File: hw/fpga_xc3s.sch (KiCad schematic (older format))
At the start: 44 parts, among them J4 JTAG, J5 GPIO2V5, J9 Conn_02x04_Odd_Even, U5 XC3S50A-VQ100, U6 AT25DF041B

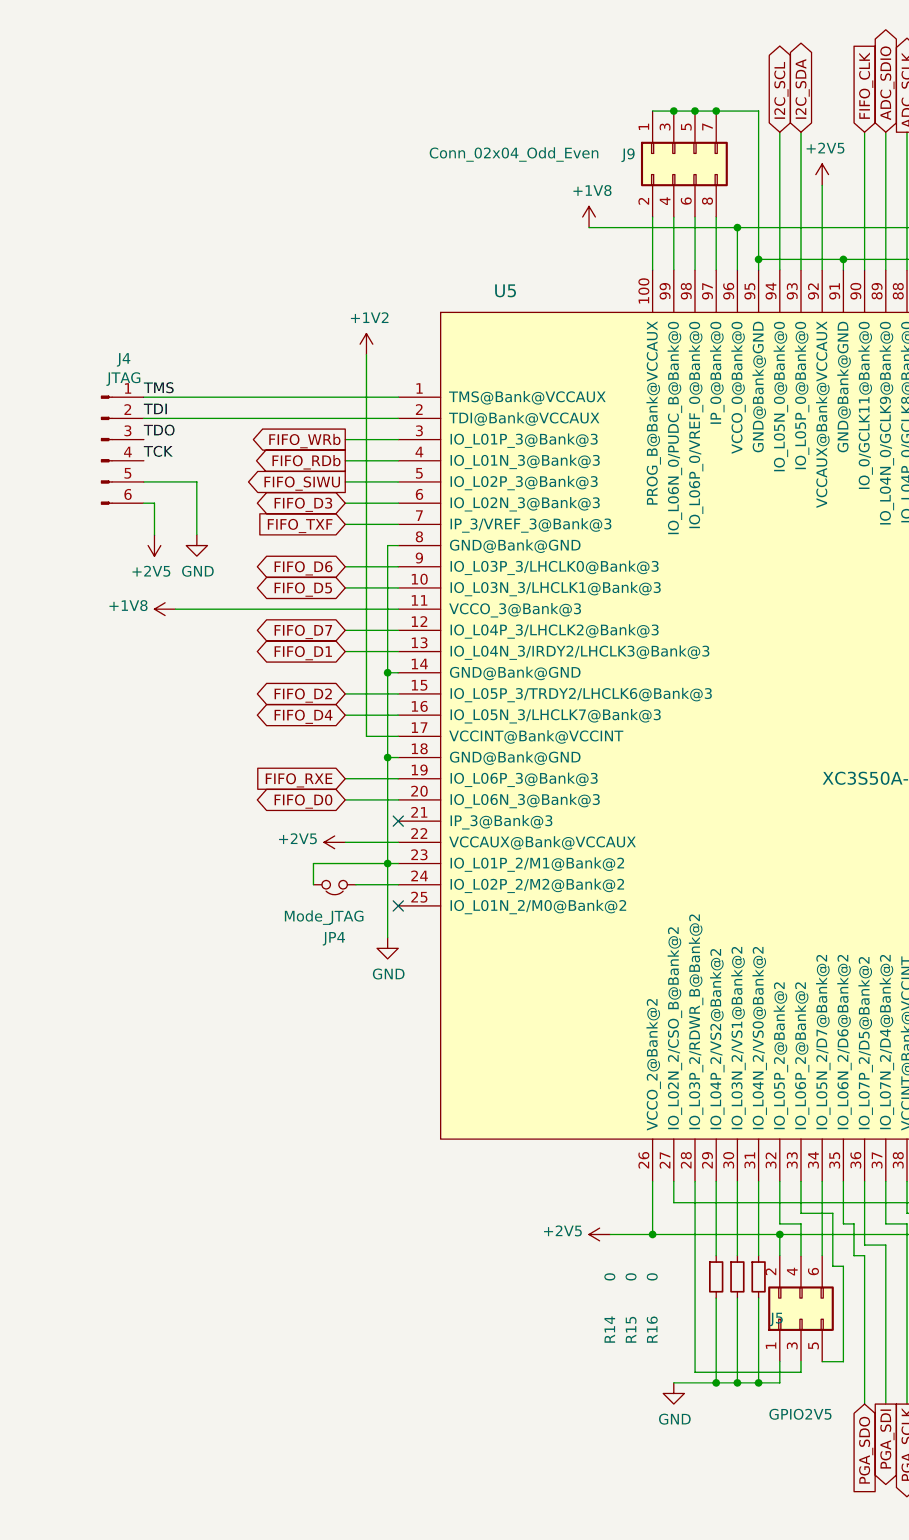
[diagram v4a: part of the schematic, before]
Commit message: everything hooked up + layed out; 0.2/0.4mm vias :-(
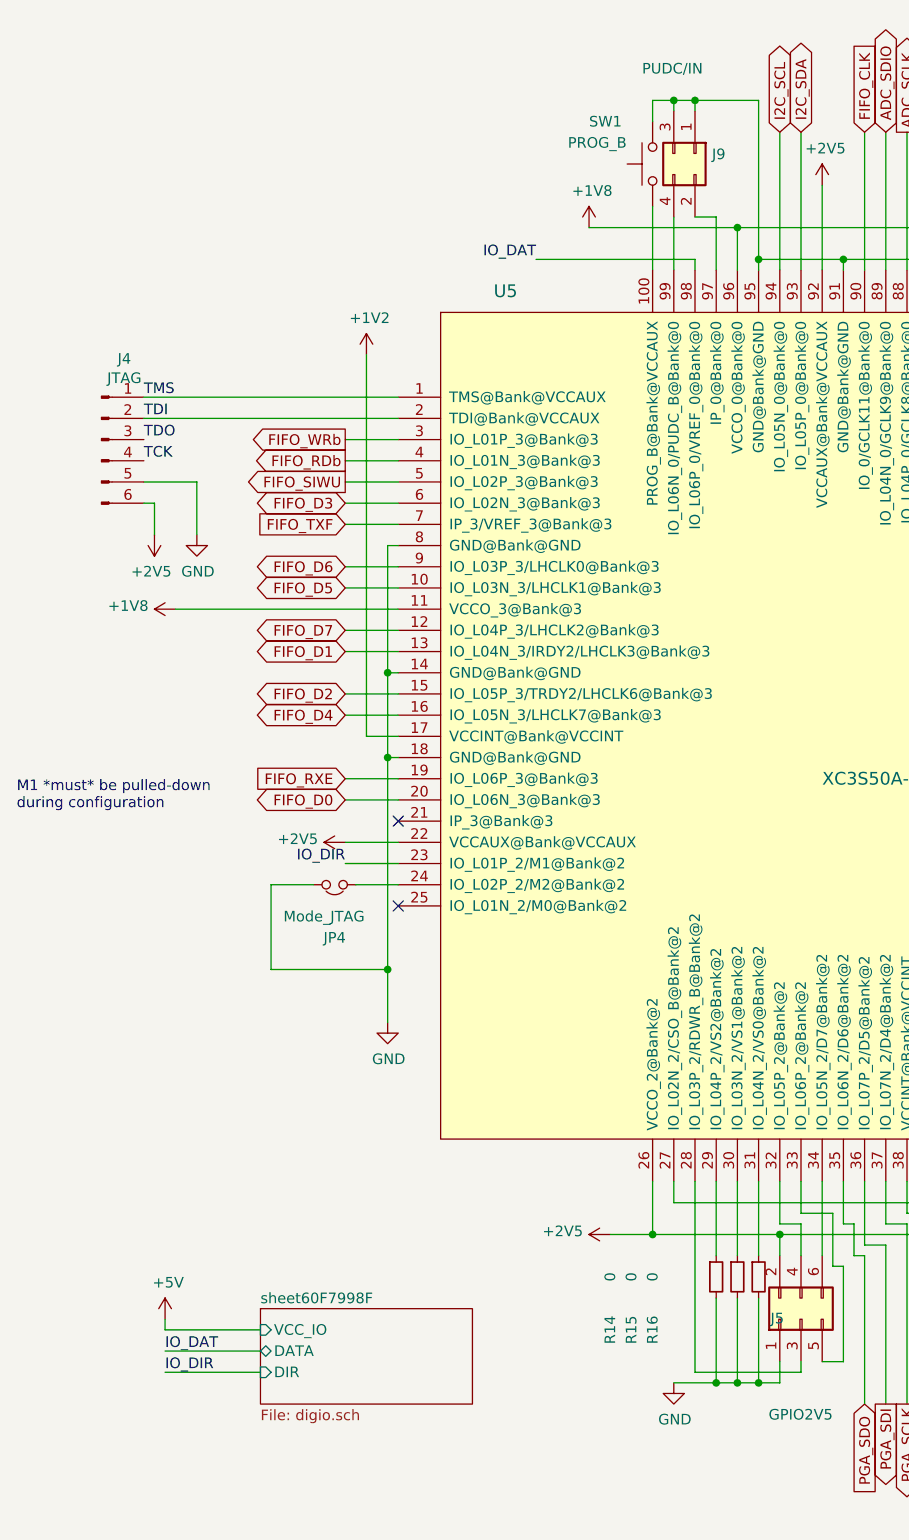
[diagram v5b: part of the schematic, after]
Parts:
- removed J9: Conn_02x04_Odd_Even, Connector_PinHeader_2.54mm:PinHeader_2x04_P2.54mm_Vertical, symbol Connector_Generic:Conn_02x04_Odd_Even
- added J9: PUDC/IN, Connector_PinHeader_2.54mm:PinHeader_2x02_P2.54mm_Vertical, symbol Connector_Generic:Conn_02x02_Odd_Even
- added SW1: PROG_B, Button_Switch_SMD:SW_SPST_PTS810, symbol Switch:SW_Push
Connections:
- net GND: now also J9.1 (Pin_1), J9.3 (Pin_3), SW1.2; no longer U5.23 (IO_L01P_2/M1@Bank@2)
- net at U5.100 (PROG_B@Bank@VCCAUX): now also SW1.1
- net at U5.99 (IO_L06N_0/PUDC_B@Bank@0): now also J9.4 (Pin_4)
- net IO_DAT: now reaches U5.98 (IO_L06P_0/VREF_0@Bank@0)
- net at U5.97 (IP_0@Bank@0): now also J9.2 (Pin_2)
- new net IO_DIR: U5.23 (IO_L01P_2/M1@Bank@2)
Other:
- note added: "M1 *must* be pulled-down\nduring configuration"
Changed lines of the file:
@@
 $Descr A4 11693 8268
 encoding utf-8
-Sheet 3 8
+Sheet 3 9
 Title ""
 Date ""
@@
 L power:GND #PWR?
 U 1 1 60AF9070
-P 2300 4950
+P 2300 5350
 AR Path="/6086F2E3/60AF9070" Ref="#PWR?"  Part="1"
 AR Path="/60AABC24/60AF9070" Ref="#PWR?"  Part="1"
-F 0 "#PWR?" H 2300 4700 50  0001 C CNN
-F 1 "GND" H 2305 4777 50  0000 C CNN
-F 2 "" H 2300 4950 50  0001 C CNN
-F 3 "" H 2300 4950 50  0001 C CNN
-	1    2300 4950
+F 0 "#PWR?" H 2300 5100 50  0001 C CNN
+F 1 "GND" H 2305 5177 50  0000 C CNN
+F 2 "" H 2300 5350 50  0001 C CNN
+F 3 "" H 2300 5350 50  0001 C CNN
+	1    2300 5350
 	1    0    0    -1
 $EndComp
@@
 Wire Wire Line
 	8050 5800 8050 6200
-NoConn ~ 2350 4800
 $Comp
 L Device:Jumper_NC_Small JP4
@@
 $EndComp
 Wire Wire Line
-	2300 4100 2300 4600
-Wire Wire Line
-	2350 4600 2300 4600
-Connection ~ 2300 4600
-Wire Wire Line
-	2300 4600 2300 4950
-Wire Wire Line
-	1950 4700 1950 4600
-Wire Wire Line
-	1950 4600 2300 4600
-Wire Wire Line
 	2350 4700 2150 4700
-Wire Wire Line
-	3550 1550 3550 1800
 $Comp
 L Connector:TestPoint TP1
@@
 $EndComp
 Wire Wire Line
-	3750 1550 3750 1800
-Wire Wire Line
 	3850 1550 3850 1800
-$Comp
-L Connector_Generic:Conn_02x04_Odd_Even J9
-U 1 1 60AB847C
-P 3650 1250
-F 0 "J9" V 3654 1430 50  0000 L CNN
-F 1 "Conn_02x04_Odd_Even" V 3650 1600 50  0000 L CNN
-F 2 "Connector_PinHeader_2.54mm:PinHeader_2x04_P2.54mm_Vertical" H 3650 1250 50  0001 C CNN
-F 3 "~" H 3650 1250 50  0001 C CNN
-	1    3650 1250
-	0    -1   1    0
-$EndComp
-Wire Wire Line
-	3550 1050 3650 1050
-Wire Wire Line
-	4050 1050 4050 1750
-Connection ~ 3650 1050
-Wire Wire Line
-	3650 1050 3750 1050
-Connection ~ 3750 1050
-Wire Wire Line
-	3750 1050 3850 1050
-Connection ~ 3850 1050
-Wire Wire Line
-	3850 1050 4050 1050
 Connection ~ 4050 1750
 Wire Wire Line
@@
 Wire Wire Line
 	4250 6250 4400 6250
+$Sheet
+S 1700 6700 1000 450
+U 60F79994
+F0 "sheet60F7998F" 50
+F1 "digio.sch" 50
+F2 "DATA" B L 1700 6900 50
+F3 "DIR" I L 1700 7000 50
+F4 "VCC_IO" I L 1700 6800 50
+$EndSheet
+Wire Wire Line
+	1700 6900 1250 6900
+Wire Wire Line
+	1700 7000 1250 7000
+Text Label 1250 6900 0    50   ~ 0
+IO_DAT
+Text Label 1250 7000 0    50   ~ 0
+IO_DIR
+$Comp
+L power:+5V #PWR?
+U 1 1 60FB29D3
+P 1250 6750
+AR Path="/6086F2E3/60FB29D3" Ref="#PWR?"  Part="1"
+AR Path="/60AABC24/60FB29D3" Ref="#PWR?"  Part="1"
+F 0 "#PWR?" H 1250 6600 50  0001 C CNN
+F 1 "+5V" H 1265 6923 50  0000 C CNN
+F 2 "" H 1250 6750 50  0001 C CNN
+F 3 "" H 1250 6750 50  0001 C CNN
+	1    1250 6750
+	1    0    0    -1
+$EndComp
+Wire Wire Line
+	1700 6800 1250 6800
+Wire Wire Line
+	1250 6800 1250 6750
+NoConn ~ 2350 4800
+Text Notes 550  4350 0    50   ~ 0
+M1 *must* be pulled-down\nduring configuration
+Wire Wire Line
+	1950 4700 1750 4700
+Wire Wire Line
+	1750 5100 2300 5100
+Wire Wire Line
+	1750 4700 1750 5100
+Connection ~ 2300 5100
+Wire Wire Line
+	2300 5100 2300 5350
+Wire Wire Line
+	2300 4100 2300 5100
+Wire Wire Line
+	2350 4600 2100 4600
+Text Label 2100 4600 2    50   ~ 0
+IO_DIR
+Wire Wire Line
+	4050 1000 3750 1000
+Wire Wire Line
+	4050 1000 4050 1750
+Wire Wire Line
+	3650 1050 3650 1000
+Connection ~ 3650 1000
+Wire Wire Line
+	3650 1000 3550 1000
+Wire Wire Line
+	3750 1050 3750 1000
+Connection ~ 3750 1000
+Wire Wire Line
+	3750 1000 3650 1000
+Wire Wire Line
+	3750 1550 3850 1550
+Wire Wire Line
+	3750 1800 3750 1750
+Wire Wire Line
+	3750 1750 3000 1750
+Text Label 3000 1750 2    50   ~ 0
+IO_DAT
+$Comp
+L Connector_Generic:Conn_02x02_Odd_Even J9
+U 1 1 61188A24
+P 3750 1250
+F 0 "J9" V 3754 1330 50  0000 L CNN
+F 1 "PUDC/IN" V 3350 1000 50  0000 L CNN
+F 2 "Connector_PinHeader_2.54mm:PinHeader_2x02_P2.54mm_Vertical" H 3750 1250 50  0001 C CNN
+F 3 "~" H 3750 1250 50  0001 C CNN
+	1    3750 1250
+	0    1    1    0
+$EndComp
+$Comp
+L Switch:SW_Push SW1
+U 1 1 61189FCC
+P 3550 1300
+F 0 "SW1" V 3750 1600 50  0000 R CNN
+F 1 "PROG_B" V 3650 1700 50  0000 R CNN
+F 2 "Button_Switch_SMD:SW_SPST_PTS810" H 3550 1500 50  0001 C CNN
+F 3 "~" H 3550 1500 50  0001 C CNN
+	1    3550 1300
+	0    -1   -1   0
+$EndComp
+Wire Wire Line
+	3550 1000 3550 1100
+Wire Wire Line
+	3550 1500 3550 1800
 $EndSCHEMATC

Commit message: prototype version
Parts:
- removed J9: PUDC/IN, Connector_PinHeader_2.54mm:PinHeader_2x02_P2.54mm_Vertical, symbol Connector_Generic:Conn_02x02_Odd_Even
- added D15: LED_Front, proj_footprints:LED_Wuerth_Sideview, symbol Device:LED_Dual_CAC
- added J12: PUDC_B/IN, Connector_PinHeader_2.54mm:PinHeader_2x02_P2.54mm_Vertical, symbol Connector_Generic:Conn_02x02_Odd_Even
- added R83, R84: 1k5, Resistor_SMD:R_0603_1608Metric, symbol Device:R_Small
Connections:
- net +2V5: now also D15.2 (A)
- net GND: now also U5.23 (IO_L01P_2/M1@Bank@2), J12.2 (Pin_2), J12.4 (Pin_4)
- net IO_DIR: now also U5.71 (IO_L05N_1@Bank@1); no longer U5.23 (IO_L01P_2/M1@Bank@2)
- net at U5.25 (IO_L01N_2/M0@Bank@2): now also R83.1
- net LED_FRONT_G: now reaches U5.52 (IO_L12P_2/D1@Bank@2)
- net LED_FRONT_G: now also R84.1
- net at U5.72 (IO_L06P_1@Bank@1): now also U5.73 (IO_L06N_1@Bank@1); no longer U5.71 (IO_L05N_1@Bank@1)
- net EXP_IO1_1V8: now reaches U5.77 (IO_L01P_0/VREF_0@Bank@0)
- net EXP_IO2_1V8: now reaches U5.78 (IO_L01N_0@Bank@0)
- net at U5.97 (IP_0@Bank@0): now also J12.3 (Pin_3)
- net at U5.99 (IO_L06N_0/PUDC_B@Bank@0): now also J12.1 (Pin_1)
- new net: D15.1 (K1), R83.2
- new net: D15.3 (K2), R84.2
- no-connect marks 9 -> 4
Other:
- note added: "M1 *must* be pulled-down,\nM0 *must* be pulled-up\nduring configuration;"
- note removed: "M1 *must* be pulled-down\nduring configuration"
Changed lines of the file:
@@
 U 1 1 6089B5A3
 P 7450 4600
-F 0 "R18" V 7700 4600 50  0000 C CNN
-F 1 "50" V 7550 4600 50  0000 C CNN
+F 0 "R18" V 7400 4450 50  0000 C CNN
+F 1 "50" V 7400 4750 50  0000 C CNN
 F 2 "Resistor_SMD:R_0603_1608Metric" H 7450 4600 50  0001 C CNN
 F 3 "~" H 7450 4600 50  0001 C CNN
@@
 Text GLabel 4550 1150 1    50   Input ~ 0
 FIFO_CLK
-NoConn ~ 7150 4700
 Wire Wire Line
 	3850 6650 3850 7050
@@
 Wire Wire Line
 	5150 1150 5150 1800
-NoConn ~ 5750 1800
-NoConn ~ 5850 1800
 Wire Wire Line
 	4250 1150 4250 1800
@@
 	1    0    0    -1
 $EndComp
-Wire Wire Line
-	3850 1550 3850 1800
-Connection ~ 4050 1750
 Wire Wire Line
 	4050 1750 4050 1800
@@
 Wire Wire Line
 	7150 3200 8100 3200
-Wire Wire Line
-	7150 2700 7450 2700
-Wire Wire Line
-	7450 2700 7450 2800
-Wire Wire Line
-	7450 2800 7150 2800
-NoConn ~ 7150 2600
 Text GLabel 2100 3300 0    50   BiDi ~ 0
 FIFO_D5
@@
 	4250 6250 4400 6250
 $Sheet
-S 1700 6700 1000 450
+S 1700 6700 850  600
 U 60F79994
 F0 "sheet60F7998F" 50
@@
 F2 "DATA" B L 1700 6900 50
 F3 "DIR" I L 1700 7000 50
-F4 "VCC_IO" I L 1700 6800 50
+F4 "VCC_IO" I R 2550 6800 50
+F5 "VCC_LOGIC" I L 1700 6800 50
 $EndSheet
 Wire Wire Line
@@
 L power:+5V #PWR?
 U 1 1 60FB29D3
-P 1250 6750
+P 2700 6650
 AR Path="/6086F2E3/60FB29D3" Ref="#PWR?"  Part="1"
 AR Path="/60AABC24/60FB29D3" Ref="#PWR?"  Part="1"
-F 0 "#PWR?" H 1250 6600 50  0001 C CNN
-F 1 "+5V" H 1265 6923 50  0000 C CNN
-F 2 "" H 1250 6750 50  0001 C CNN
-F 3 "" H 1250 6750 50  0001 C CNN
-	1    1250 6750
+F 0 "#PWR?" H 2700 6500 50  0001 C CNN
+F 1 "+5V" H 2715 6823 50  0000 C CNN
+F 2 "" H 2700 6650 50  0001 C CNN
+F 3 "" H 2700 6650 50  0001 C CNN
+	1    2700 6650
 	1    0    0    -1
 $EndComp
@@
 Wire Wire Line
 	1250 6800 1250 6750
-NoConn ~ 2350 4800
 Text Notes 550  4350 0    50   ~ 0
-M1 *must* be pulled-down\nduring configuration
+M1 *must* be pulled-down,\nM0 *must* be pulled-up\nduring configuration;
 Wire Wire Line
 	1950 4700 1750 4700
@@
 	2300 5100 2300 5350
 Wire Wire Line
-	2300 4100 2300 5100
-Wire Wire Line
-	2350 4600 2100 4600
-Text Label 2100 4600 2    50   ~ 0
+	2300 4100 2300 4600
+Text Label 7600 2800 0    50   ~ 0
 IO_DIR
 Wire Wire Line
-	4050 1000 3750 1000
-Wire Wire Line
-	4050 1000 4050 1750
-Wire Wire Line
 	3650 1050 3650 1000
-Connection ~ 3650 1000
 Wire Wire Line
 	3650 1000 3550 1000
-Wire Wire Line
-	3750 1050 3750 1000
-Connection ~ 3750 1000
-Wire Wire Line
-	3750 1000 3650 1000
-Wire Wire Line
-	3750 1550 3850 1550
 Wire Wire Line
 	3750 1800 3750 1750
@@
 IO_DAT
 $Comp
-L Connector_Generic:Conn_02x02_Odd_Even J9
-U 1 1 61188A24
-P 3750 1250
-F 0 "J9" V 3754 1330 50  0000 L CNN
-F 1 "PUDC/IN" V 3350 1000 50  0000 L CNN
-F 2 "Connector_PinHeader_2.54mm:PinHeader_2x02_P2.54mm_Vertical" H 3750 1250 50  0001 C CNN
-F 3 "~" H 3750 1250 50  0001 C CNN
-	1    3750 1250
-	0    1    1    0
-$EndComp
-$Comp
 L Switch:SW_Push SW1
 U 1 1 61189FCC
 P 3550 1300
-F 0 "SW1" V 3750 1600 50  0000 R CNN
-F 1 "PROG_B" V 3650 1700 50  0000 R CNN
+F 0 "SW1" H 4050 1300 50  0000 R CNN
+F 1 "PROG_B" H 4350 1300 50  0000 R CNN
 F 2 "Button_Switch_SMD:SW_SPST_PTS810" H 3550 1500 50  0001 C CNN
 F 3 "~" H 3550 1500 50  0001 C CNN
@@
 	0    -1   -1   0
 $EndComp
+$Comp
+L Device:LED_Dual_CAC D15
+U 1 1 60F9CC93
+P 1000 5400
+F 0 "D15" V 954 5688 50  0000 L CNN
+F 1 "LED_Front" V 1045 5688 50  0000 L CNN
+F 2 "proj_footprints:LED_Wuerth_Sideview" H 1050 5400 50  0001 C CNN
+F 3 "~" H 1050 5400 50  0001 C CNN
+	1    1000 5400
+	0    1    1    0
+$EndComp
+$Comp
+L power:+2V5 #PWR?
+U 1 1 60F9E431
+P 1000 5000
+AR Path="/6086F2E3/60F9E431" Ref="#PWR?"  Part="1"
+AR Path="/60AABC24/60F9E431" Ref="#PWR?"  Part="1"
+F 0 "#PWR?" H 1000 4850 50  0001 C CNN
+F 1 "+2V5" V 1015 5128 50  0000 L CNN
+F 2 "" H 1000 5000 50  0001 C CNN
+F 3 "" H 1000 5000 50  0001 C CNN
+	1    1000 5000
+	1    0    0    -1
+$EndComp
+Wire Wire Line
+	1000 5000 1000 5100
+$Comp
+L Device:R_Small R83
+U 1 1 60FB2976
+P 1350 5700
+F 0 "R83" V 1450 5700 50  0000 C CNN
+F 1 "1k5" V 1250 5700 50  0000 C CNN
+F 2 "Resistor_SMD:R_0603_1608Metric" H 1350 5700 50  0001 C CNN
+F 3 "~" H 1350 5700 50  0001 C CNN
+F 4 " RC0603FR-071K5L " V 1350 5700 50  0001 C CNN "Part"
+F 5 "Yageo" V 1350 5700 50  0001 C CNN "Manufacturer"
+	1    1350 5700
+	0    1    -1   0
+$EndComp
+Wire Wire Line
+	1100 5700 1250 5700
+Wire Wire Line
+	2350 4800 1450 4800
+Wire Wire Line
+	2700 6650 2700 6800
+Wire Wire Line
+	2700 6800 2550 6800
+Wire Wire Line
+	7150 2600 7450 2600
+Wire Wire Line
+	7450 2600 7450 2700
+Wire Wire Line
+	7450 2700 7150 2700
+Wire Wire Line
+	7150 2800 7600 2800
+Wire Wire Line
+	2350 4600 2300 4600
+Connection ~ 2300 4600
+Wire Wire Line
+	2300 4600 2300 5100
+$Comp
+L power:+1V8 #PWR?
+U 1 1 6104E276
+P 1250 6750
+AR Path="/6086F2E3/6104E276" Ref="#PWR?"  Part="1"
+AR Path="/60AABC24/6104E276" Ref="#PWR?"  Part="1"
+F 0 "#PWR?" H 1250 6600 50  0001 C CNN
+F 1 "+1V8" H 1265 6923 50  0000 C CNN
+F 2 "" H 1250 6750 50  0001 C CNN
+F 3 "" H 1250 6750 50  0001 C CNN
+	1    1250 6750
+	1    0    0    -1
+$EndComp
+$Comp
+L Device:R_Small R84
+U 1 1 6104F4FE
+P 1350 6000
+F 0 "R84" V 1450 6000 50  0000 C CNN
+F 1 "1k5" V 1250 6000 50  0000 C CNN
+F 2 "Resistor_SMD:R_0603_1608Metric" H 1350 6000 50  0001 C CNN
+F 3 "~" H 1350 6000 50  0001 C CNN
+F 4 " RC0603FR-071K5L " V 1350 6000 50  0001 C CNN "Part"
+F 5 "Yageo" V 1350 6000 50  0001 C CNN "Manufacturer"
+	1    1350 6000
+	0    1    -1   0
+$EndComp
+Wire Wire Line
+	1450 4800 1450 5700
+Wire Wire Line
+	900  5700 900  6000
+Wire Wire Line
+	900  6000 1250 6000
+Text Label 1600 6000 0    50   ~ 0
+LED_FRONT_G
+Wire Wire Line
+	1600 6000 1450 6000
+Text Label 7350 4700 0    50   ~ 0
+LED_FRONT_G
+Wire Wire Line
+	7350 4700 7150 4700
+Text GLabel 5850 1150 1    50   BiDi ~ 0
+EXP_IO1_1V8
+$Comp
+L power:GND #PWR?
+U 1 1 61391125
+P 3250 1000
+AR Path="/6086F2E3/61391125" Ref="#PWR?"  Part="1"
+AR Path="/60AABC24/61391125" Ref="#PWR?"  Part="1"
+F 0 "#PWR?" H 3250 750 50  0001 C CNN
+F 1 "GND" H 3255 827 50  0000 C CNN
+F 2 "" H 3250 1000 50  0001 C CNN
+F 3 "" H 3250 1000 50  0001 C CNN
+	1    3250 1000
+	1    0    0    -1
+$EndComp
+Wire Wire Line
+	3250 1000 3550 1000
+Connection ~ 3550 1000
+Text GLabel 5750 1150 1    50   BiDi ~ 0
+EXP_IO2_1V8
+Wire Wire Line
+	5850 1150 5850 1800
+Wire Wire Line
+	5750 1150 5750 1800
+Wire Wire Line
+	3750 1050 3750 1000
+Wire Wire Line
+	3750 1000 3650 1000
+Connection ~ 3650 1000
+Wire Wire Line
+	3850 1800 3850 1700
+Wire Wire Line
+	3850 1700 3750 1700
+Wire Wire Line
+	3750 1700 3750 1550
+Wire Wire Line
+	3550 1500 3550 1800
 Wire Wire Line
 	3550 1000 3550 1100
-Wire Wire Line
-	3550 1500 3550 1800
+$Comp
+L Connector_Generic:Conn_02x02_Odd_Even J12
+U 1 1 6102674D
+P 3650 1350
+F 0 "J12" V 3654 1162 50  0000 R CNN
+F 1 "PUDC_B/IN" H 4500 1300 50  0000 R CNN
+F 2 "Connector_PinHeader_2.54mm:PinHeader_2x02_P2.54mm_Vertical" H 3650 1350 50  0001 C CNN
+F 3 "~" H 3650 1350 50  0001 C CNN
+	1    3650 1350
+	0    -1   -1   0
+$EndComp
 $EndSCHEMATC
